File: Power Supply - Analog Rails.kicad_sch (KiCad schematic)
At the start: 30 parts, among them IC3 LTC6655LNBHMS8-2.5#PBF, IC5 LT8362EMSE#PBF, IC7 LTC6655BHMS8-5#PBF, IC8 LT3045EDD-1#TRPBF, IC9 LT3045EDD-1#TRPBF

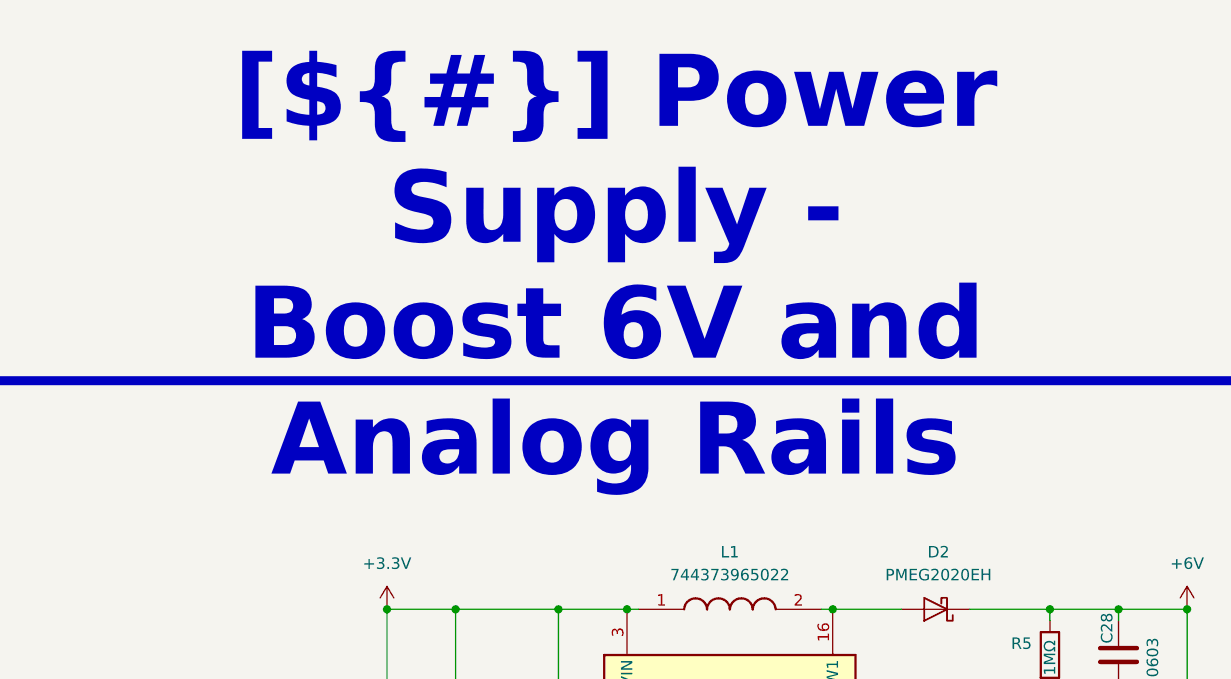
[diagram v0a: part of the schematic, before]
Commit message: Fill template pages: block diagram, power sequencing, cover notes, architecture
- Block Diagram redrawn from the real design: phase path (MR60PW, shunts),
  current and voltage channels with their gains and bandwidths, AD7606C-18,
  power chain, target specifications
- Power - Sequencing: start-up curves taken from the LTspice simulations
  (boost soft-start, analog rails) and rail table with sources, levels
  and timings
- Cover page: real design notes instead of the template examples
- Project Architecture: power-supply block documented, contiguous page
  numbers (Power Supply is page 6)
- Revision History: one column fed by the [Unreleased] changelog section
- sheet titles shortened so they fit the cover-page index: INA241 - Phase
  Sensing, Power Supply - Analog Rails

Sheet-level polylines carry no fill attribute (KiBot schematic reader).

Co-Authored-By: Claude Opus 5.5 <noreply@anthropic.com>
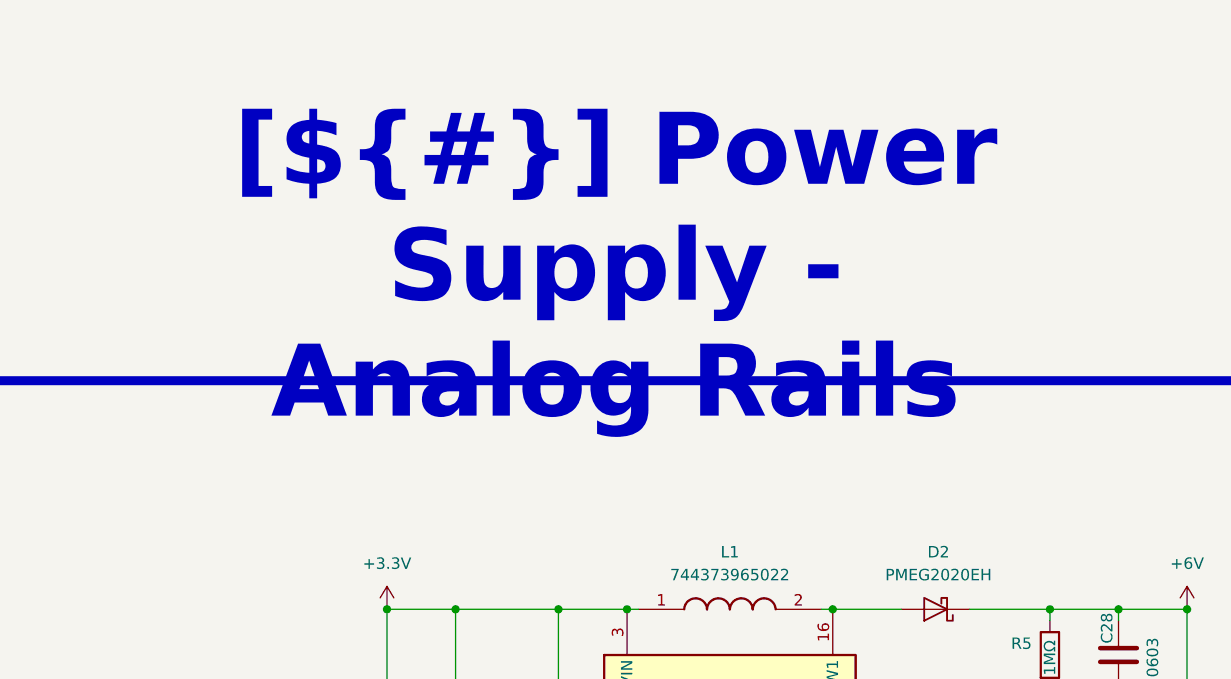
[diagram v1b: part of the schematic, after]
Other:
- title: Power Supply - Boost 6V and Analog Rails -> Power Supply - Analog Rails
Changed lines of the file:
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@@
 	(paper "A3")
 	(title_block
-		(title "Power Supply - Boost 6V and Analog Rails")
+		(title "Power Supply - Analog Rails")
 		(date "2026-10-05")
 		(rev "${REVISION}")

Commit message: Fix the +2.5VA reference, add XT60PW-M connectors, predict measurement quality
- IC3: LTC6655LN-2.5 replaced by the standard LTC6655-2.5, pin 6 is now
  VOUT_S tied to VOUT_F (the LN version has NR on that pin)
- R12: 49.9k -> 24.9k on the SET pin of IC9, +2.5VA = 2.500 V instead of
  2.549 V; both points removed from the README design review
- J5, J6: two Amass XT60PW-M added on the Connectors sheet and on the PCB,
  with symbol, footprint and 3D model in lib/. Their power pins are not
  wired yet
- Simulations 07 (ESC PWM waveforms through both channels) and 08 (Monte
  Carlo on the tolerances), analysed by measurement_quality.py into
  measurement_quality.md; plot style shared in plotstyle.py
- Simulations 01, 02, 04, results.md and their figures redone for the
  corrected rail
- README, README template and CHANGELOG updated; all sheets re-saved from
  KiCad

Co-Authored-By: Claude Opus 5.5 <noreply@anthropic.com>
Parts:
- IC3: value LTC6655LNBHMS8-2.5#PBF -> LTC6655BHMS8-2.5#PBF; symbol PhaseSense-8586:LTC6655LNBHMS8-2.5#PBF -> PhaseSense-8586:LTC6655BHMS8-2.5#PBF; Arrow Part Number LTC6655LNBHMS8-2.5#PBF -> LTC6655BHMS8-2.5#PBF; Arrow Price/Stock https://www.arrow.com/en/products/ltc6655lnbhms8-2.5pbf/ana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 -> (none); Manufacturer_Part_Number LTC6655LNBHMS8-2.5#PBF -> LTC6655BHMS8-2.5#PBF; Mouser Part Number 584-6655LNBHMS825PBF -> (none); Mouser Price/Stock https://www.mouser.co.uk/ProductDetail/Analog-Devices/LTC66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 -> (none)
- R12: value 49.9kΩ -> 24.9kΩ
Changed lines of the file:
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@@
 	(title_block
 		(title "Power Supply - Analog Rails")
-		(date "2026-10-05")
+		(date "2026-10-06")
 		(rev "${REVISION}")
 		(company "${COMPANY}")
@@
 	)
 	(symbol
-		(lib_id "PhaseSense-8586:LTC6655LNBHMS8-2.5#PBF")
+		(lib_id "PhaseSense-8586:LTC6655BHMS8-2.5#PBF")
 		(at 245.11 205.74 0)
 		(unit 1)
@@
 			)
 		)
-		(property "Value" "LTC6655LNBHMS8-2.5#PBF"
+		(property "Value" "LTC6655BHMS8-2.5#PBF"
 			(at 261.62 200.66 0)
 			(show_name no)
@@
 			)
 		)
-		(property "Manufacturer_Part_Number" "LTC6655LNBHMS8-2.5#PBF"
+		(property "Manufacturer_Part_Number" "LTC6655BHMS8-2.5#PBF"
 			(at 274.32 800.66 0)
 			(hide yes)
@@
 			)
 		)
-		(property "Mouser Part Number" "584-6655LNBHMS825PBF"
+		(property "Mouser Part Number" ""
 			(at 274.32 900.66 0)
 			(hide yes)
@@
 			)
 		)
-		(property "Mouser Price/Stock" "https://www.mouser.co.uk/ProductDetail/Analog-Devices/LTC6655LNBHMS8-2.5PBF?qs=0lSvoLzn4L%252BRohUD3M%252BeWQ%3D%3D"
+		(property "Mouser Price/Stock" ""
 			(at 274.32 1000.66 0)
 			(hide yes)
@@
 			)
 		)
-		(property "Arrow Part Number" "LTC6655LNBHMS8-2.5#PBF"
+		(property "Arrow Part Number" "LTC6655BHMS8-2.5#PBF"
 			(at 274.32 1100.66 0)
 			(hide yes)
@@
 			)
 		)
-		(property "Arrow Price/Stock" "https://www.arrow.com/en/products/ltc6655lnbhms8-2.5pbf/analog-devices.html?utm_currency=USD&region=nac"
+		(property "Arrow Price/Stock" ""
 			(at 274.32 1200.66 0)
 			(hide yes)
@@
 			)
 		)
-		(property "Value" "49.9kΩ"
+		(property "Value" "24.9kΩ"
 			(at 293.37 215.646 90)
 			(show_name no)

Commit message: Rename the project to OPEN_PHASE
PhaseSense-8586 was named after the first parts of the design (INA240 +
ADS8586S), which are no longer on the board. OPEN_PHASE follows
OPEN_WEIGHT, the other OPEN THRUST LAB board.

- project files: OPEN_PHASE.kicad_pro / _sch / _pcb / _prl / _dru
- libraries: lib/lib_sym/OPEN_PHASE.kicad_sym and
  lib/lib_fp/OPEN_PHASE.pretty, nickname OPEN_PHASE in both tables, in
  every lib_id and in every footprint of the PCB
- project name of every symbol and sheet instance, so the reference
  designators are kept
- PROJECT_NAME and GIT_URL in the project and in kibot_main.yaml, README
  and its template, CHANGELOG, LTspice headers and their generator
- the README note now says the project was first published as
  PhaseSense-8586

The GitHub repository is now foukouda/OPEN_PHASE. The board name
PHASETRACKER is unchanged. The netlist, ERC and DRC reports are the same
before and after the rename.

Co-Authored-By: Claude Opus 5.5 <noreply@anthropic.com>
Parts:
- C11, C12, C22, C23, C24, C26, C27, C28, C8, C9: footprint PhaseSense-8586:C_0603_1608Metric -> OPEN_PHASE:C_0603_1608Metric; symbol PhaseSense-8586:C -> OPEN_PHASE:C
- C13, C19: footprint PhaseSense-8586:C_0805_2012Metric -> OPEN_PHASE:C_0805_2012Metric; symbol PhaseSense-8586:C -> OPEN_PHASE:C
- C14, C15: footprint PhaseSense-8586:C_0805_2012Metric -> OPEN_PHASE:C_0805_2012Metric; symbol PhaseSense-8586:C_4T -> OPEN_PHASE:C_4T
- C30: footprint PhaseSense-8586:C_1206_3216Metric_Pad1.33x1.80mm_HandSolder -> OPEN_PHASE:C_1206_3216Metric_Pad1.33x1.80mm_HandSolder; symbol PhaseSense-8586:C -> OPEN_PHASE:C
- D2: footprint PhaseSense-8586:D_SOD-123F -> OPEN_PHASE:D_SOD-123F; symbol PhaseSense-8586:PMEG2020EH -> OPEN_PHASE:PMEG2020EH
- IC3: footprint PhaseSense-8586:SOP65P490X110-8N -> OPEN_PHASE:SOP65P490X110-8N; symbol PhaseSense-8586:LTC6655BHMS8-2.5#PBF -> OPEN_PHASE:LTC6655BHMS8-2.5#PBF
- IC5: footprint PhaseSense-8586:LT8362EMSEPBF -> OPEN_PHASE:LT8362EMSEPBF; symbol PhaseSense-8586:LT8362EMSE#PBF -> OPEN_PHASE:LT8362EMSE#PBF
- IC7: footprint PhaseSense-8586:SOP65P490X110-8N -> OPEN_PHASE:SOP65P490X110-8N; symbol PhaseSense-8586:LTC6655BHMS8-5#PBF -> OPEN_PHASE:LTC6655BHMS8-5#PBF
- IC8, IC9: footprint PhaseSense-8586:SON45P300X300X80-13N-D -> OPEN_PHASE:SON45P300X300X80-13N-D; symbol PhaseSense-8586:LT3045EDD-1#TRPBF -> OPEN_PHASE:LT3045EDD-1#TRPBF
- L1: footprint PhaseSense-8586:INDPM135125X620N -> OPEN_PHASE:INDPM135125X620N; symbol PhaseSense-8586:744373965022 -> OPEN_PHASE:744373965022
- R11, R12, R14, R2, R3, R5, R6, R8: footprint PhaseSense-8586:R_0603_1608Metric -> OPEN_PHASE:R_0603_1608Metric; symbol PhaseSense-8586:R -> OPEN_PHASE:R

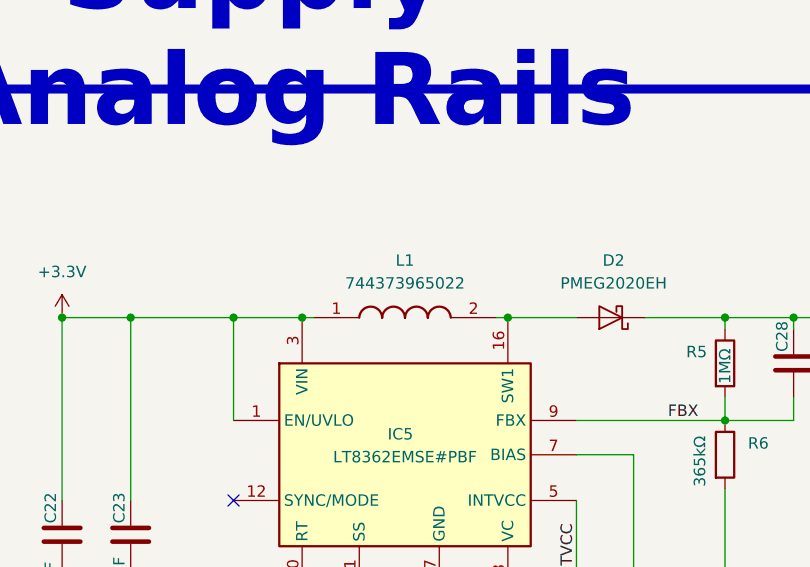
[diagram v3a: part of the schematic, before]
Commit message: Smaller boost inductor, white board, openEMS and thermal simulations
- L1: Wurth 744373965022 (13.5 x 12.5 mm) -> WE-MAPI 4030 74438357022
  (2.2 uH, 4.1 x 4.1 x 3.1 mm, Isat 4.6 A at -10 %, above the 3.1 A LT8362
  switch limit). Footprint and STEP from the KiCad library, copied to lib/.
- Board: solder mask white (custom opaque #F4F4F0F5, the KiCad "White"
  preset renders pink over copper), silkscreen black. kibot_globals.yaml
  names the colours so the fabrication notes print WHITE / BLACK.
- Simulation/openEMS: inductance of the PBV shunts seen by the INA241
  inputs on the routed copper (results.md, figures in Images/Simulation).
- Simulation/Thermal: current density and temperature of the power paths.
- LTspice simulations, figures and README updated; sim07 DC bus figure.
- 3D animation (Images/OPEN_PHASE.mp4, OPEN_PHASE-spin.gif) on the white board.
- XT60PW-F footprint and model, bottom silkscreen cartouches.

Co-Authored-By: Claude Opus 5.5 <noreply@anthropic.com>
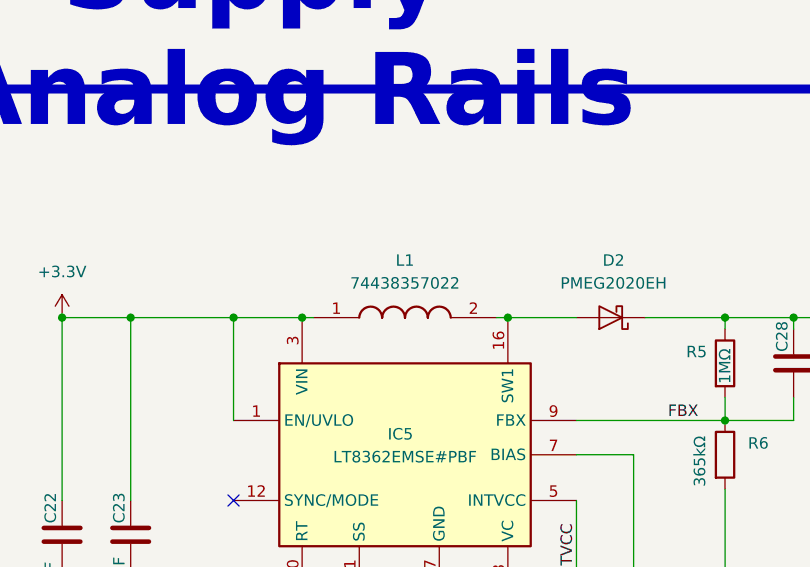
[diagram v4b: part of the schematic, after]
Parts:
- L1: value 744373965022 -> 74438357022; footprint OPEN_PHASE:INDPM135125X620N -> OPEN_PHASE:L_Wuerth_MAPI-4030; symbol OPEN_PHASE:744373965022 -> OPEN_PHASE:74438357022; Height 6.2 -> 3.1; Manufacturer_Part_Number 744373965022 -> 74438357022; Mouser Part Number 710-744373965022 -> 710-74438357022; Mouser Price/Stock https://www.mouser.co.uk/ProductDetail/Wurth-Elektronik/744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 -> https://www.mouser.com/ProductDetail/Wurth-Elektronik/74438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
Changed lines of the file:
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@@
 	)
 	(symbol
-		(lib_id "OPEN_PHASE:744373965022")
+		(lib_id "OPEN_PHASE:74438357022")
 		(at 212.09 64.77 0)
 		(unit 1)
@@
 			)
 		)
-		(property "Value" "744373965022"
+		(property "Value" "74438357022"
 			(at 222.25 60.96 0)
 			(show_name no)
@@
 			)
 		)
-		(property "Footprint" "OPEN_PHASE:INDPM135125X620N"
+		(property "Footprint" "OPEN_PHASE:L_Wuerth_MAPI-4030"
 			(at 228.6 160.96 0)
 			(hide yes)
@@
 			)
 		)
-		(property "Datasheet" "https://www.we-online.com/catalog/datasheet/744373965022.pdf"
+		(property "Datasheet" "https://www.we-online.com/components/products/datasheet/74438357022.pdf"
 			(at 228.6 260.96 0)
 			(hide yes)
@@
 			)
 		)
-		(property "Description" "WE-LHMI SMT Power Inductor Size 1365; L = 2,2 H ; IR = 17 A; Isat = 41,1 A; RDC = 4,2 m"
+		(property "Description" "WE-MAPI SMT Power Inductor Size 4030; L = 2,2 µH; IRP,40K = 7,1 A; Isat,10% = 4,6 A; Isat,30% = 9,2 A; RDC = 22 mΩ typ / 26 mΩ max"
 			(at 212.09 64.77 0)
 			(hide yes)
@@
 			)
 		)
-		(property "Height" "6.2"
+		(property "Height" "3.1"
 			(at 228.6 460.96 0)
 			(hide yes)
@@
 			)
 		)
-		(property "Manufacturer_Part_Number" "744373965022"
+		(property "Manufacturer_Part_Number" "74438357022"
 			(at 228.6 660.96 0)
 			(hide yes)
@@
 			)
 		)
-		(property "Mouser Part Number" "710-744373965022"
+		(property "Mouser Part Number" "710-74438357022"
 			(at 228.6 760.96 0)
 			(hide yes)
@@
 			)
 		)
-		(property "Mouser Price/Stock" "https://www.mouser.co.uk/ProductDetail/Wurth-Elektronik/744373965022?qs=BZBei1rCqCC1TQlqJ2wRyg%3D%3D"
+		(property "Mouser Price/Stock" "https://www.mouser.com/ProductDetail/Wurth-Elektronik/74438357022"
 			(at 228.6 860.96 0)
 			(hide yes)
